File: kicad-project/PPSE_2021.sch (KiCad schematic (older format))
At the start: 0 parts

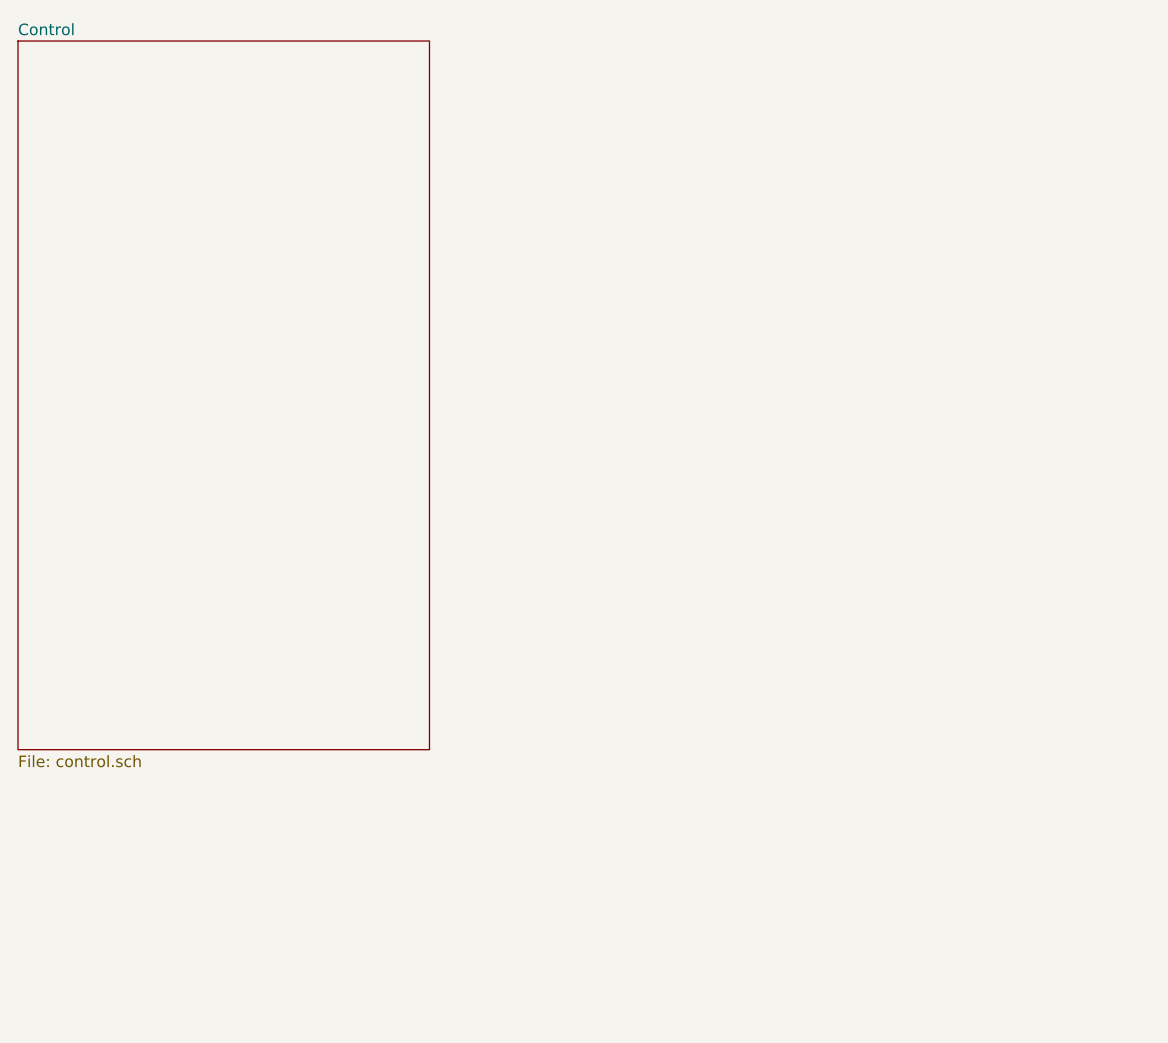
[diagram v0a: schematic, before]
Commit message: sch: add notes and circuits from 2022/03/10 lecture
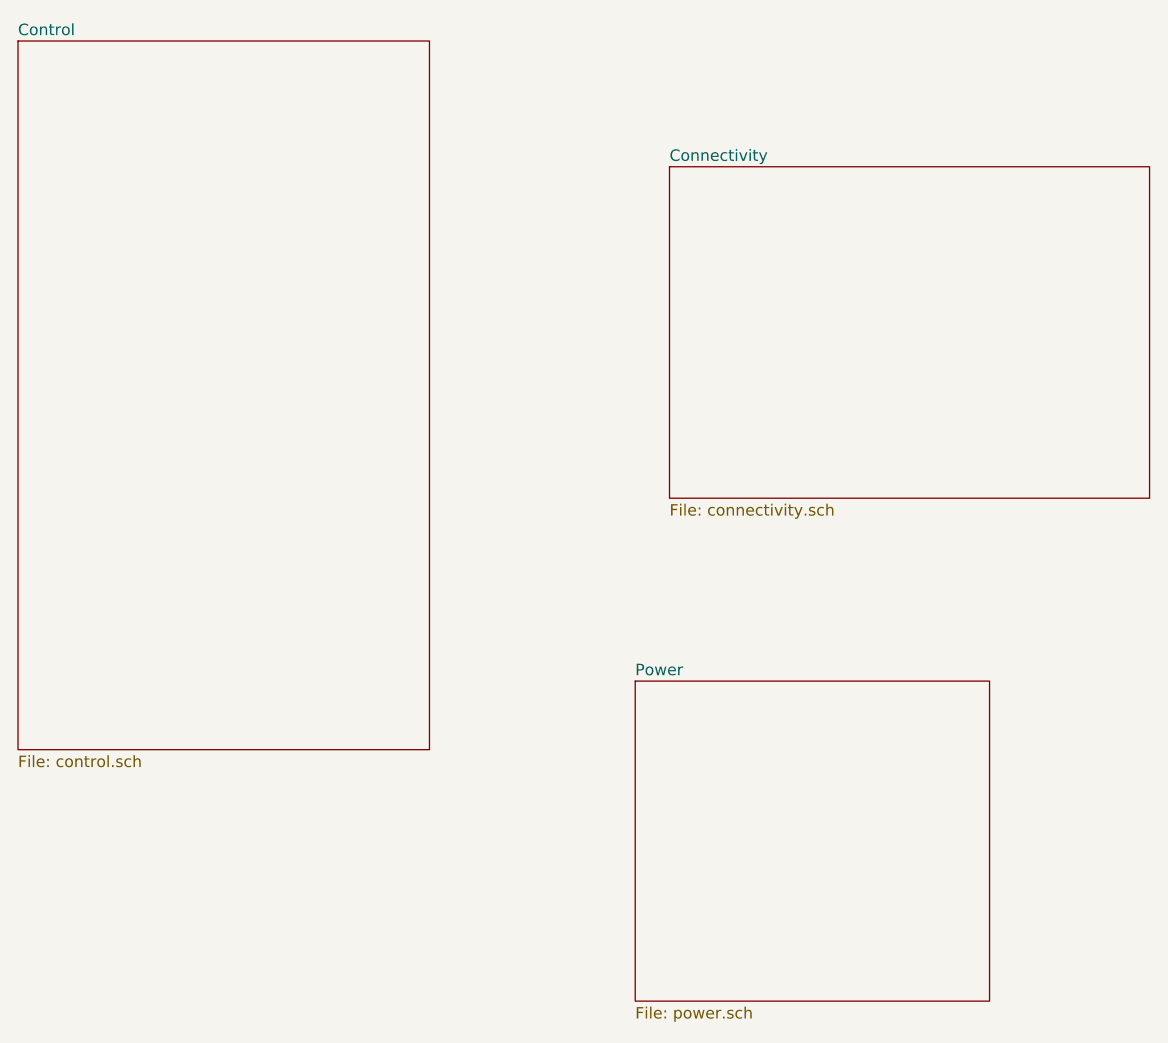
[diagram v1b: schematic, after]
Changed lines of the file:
@@
 $Descr A4 11693 8268
 encoding utf-8
-Sheet 1 2
+Sheet 1 4
 Title ""
 Date ""
@@
 F1 "control.sch" 50
 $EndSheet
+$Sheet
+S 4850 2100 2100 1450
+U 622B4158
+F0 "Connectivity" 50
+F1 "connectivity.sch" 50
+$EndSheet
+$Sheet
+S 4700 4350 1550 1400
+U 622D0E2D
+F0 "Power" 50
+F1 "power.sch" 50
+$EndSheet
 $EndSCHEMATC

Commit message: sch: add gps
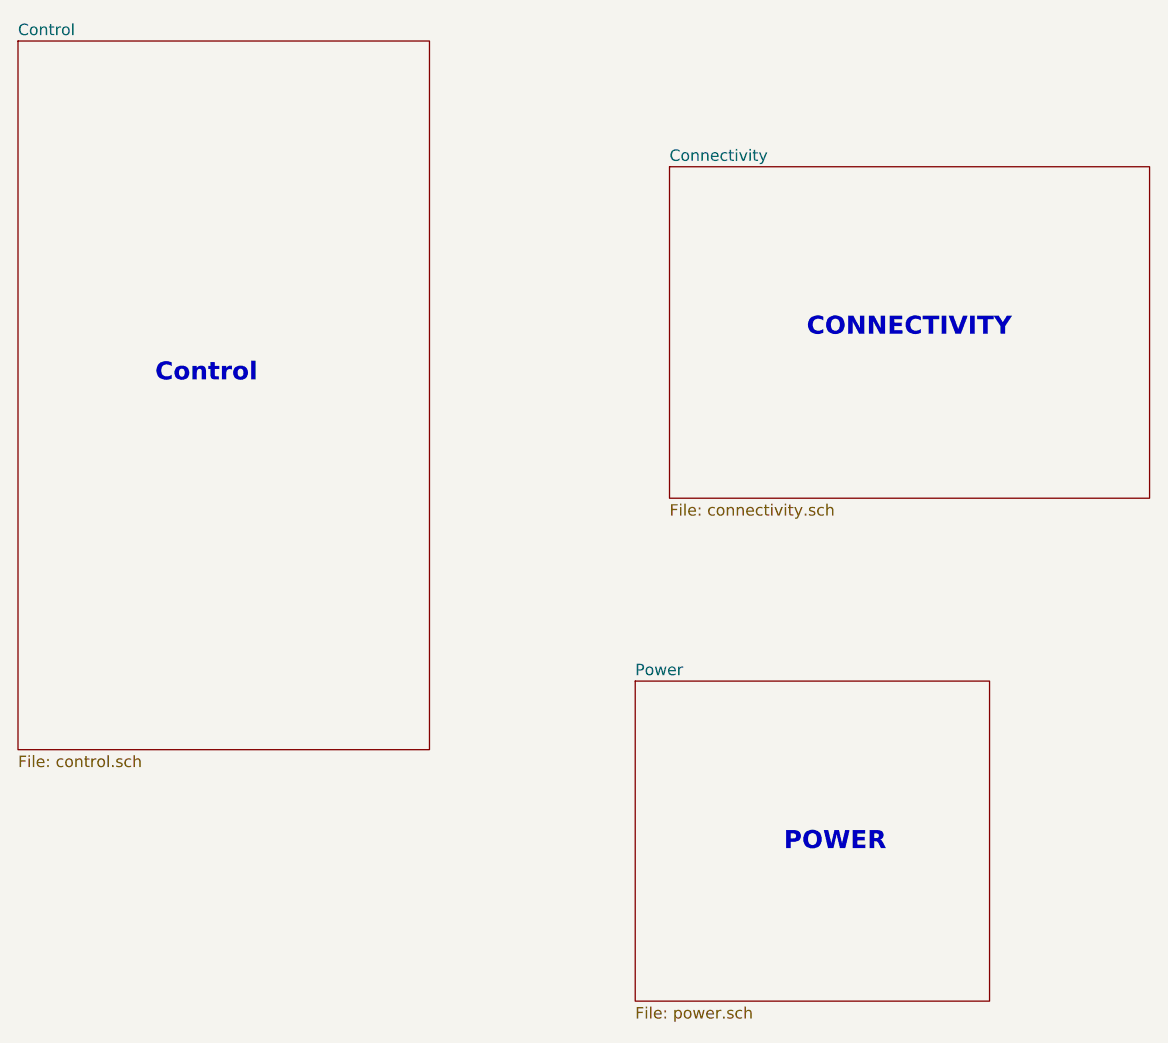
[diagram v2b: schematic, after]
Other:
- note added: "CONNECTIVITY"
- note added: "Control"
- note added: "POWER"
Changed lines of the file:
@@
 F1 "power.sch" 50
 $EndSheet
+Text Notes 5450 2850 0    79   ~ 16
+CONNECTIVITY
+Text Notes 5350 5100 0    79   ~ 16
+POWER
+Text Notes 2600 3050 0    79   ~ 16
+Control
 $EndSCHEMATC
